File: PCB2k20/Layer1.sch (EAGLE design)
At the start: 279 parts, among them J1 XT30PB-F, J10 14AWG, J11 14AWG, J13 14AWG, J14 14AWG, J15 14AWG, J16 14AWG, J17 14AWG, J18 14AWG, J19 14AWG, J20 14AWG, J3 14AWG, J4 14AWG, J5 14AWG, J6 14AWG, J7 14AWG, J8 14AWG, J9 14AWG, Q1M1 AOD482, Q1M2 AOD482, Q1M3 AOD482, Q1M4 AOD482, U1M1 VNH5019, U1M2 VNH5019, U1M3 VNH5019, U1M4 VNH5019, X1 BM10B-SRSS-TB

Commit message: add gerbers, please everything turn out well!
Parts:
- added J21, U$29: 14AWG, JH:14AWG
- 2L1: value SWPA8040/10uH -> 10uH
- 3C4: value 1500uF -> 1000uF/63V
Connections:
- net GND: now also J21.1, U$29.1
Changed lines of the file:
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@@
 <part name="2C3" library="JH" library_urn="urn:adsk.eagle:library:6027132" deviceset="CAPACITOR" device="0603" package3d_urn="urn:adsk.eagle:package:15441226/3" value="10.0nF"/>
 <part name="2D1" library="SparkFun-DiscreteSemi" library_urn="urn:adsk.eagle:library:514" deviceset="DIODE-SCHOTTKY" device="-B340A" package3d_urn="urn:adsk.eagle:package:38443/1" value="3A/40V/500mV"/>
-<part name="2L1" library="JH" library_urn="urn:adsk.eagle:library:6027132" deviceset="INDUCTOR" device="SWPA8040" package3d_urn="urn:adsk.eagle:package:15402033/4" value="SWPA8040/10uH"/>
+<part name="2L1" library="JH" library_urn="urn:adsk.eagle:library:6027132" deviceset="INDUCTOR" device="SWPA8040" package3d_urn="urn:adsk.eagle:package:15402033/4" value="10uH"/>
 <part name="2R1" library="JH" library_urn="urn:adsk.eagle:library:6027132" deviceset="RESISTOR" device="0603" package3d_urn="urn:adsk.eagle:package:15441228/3" value="10k"/>
 <part name="2C4" library="rcl" library_urn="urn:adsk.eagle:library:334" deviceset="CPOL-US" device="D/7343-31R" package3d_urn="urn:adsk.eagle:package:23417/2" value="220uF"/>
@@
 <part name="SUPPLY25" library="SparkFun-PowerSymbols" library_urn="urn:adsk.eagle:library:530" deviceset="12V" device=""/>
 <part name="SUPPLY26" library="SparkFun-PowerSymbols" library_urn="urn:adsk.eagle:library:530" deviceset="3.3V" device=""/>
-<part name="CONN_M1" library="JH" library_urn="urn:adsk.eagle:library:6027132" deviceset="XT30" device="PB-F" package3d_urn="urn:adsk.eagle:package:15925142/4"/>
+<part name="CONN_M1" library="JH" library_urn="urn:adsk.eagle:library:6027132" deviceset="XT30" device="PB-F" package3d_urn="urn:adsk.eagle:package:15925142/7"/>
 <part name="U$4" library="JH" library_urn="urn:adsk.eagle:library:6027132" deviceset="74LVC2G" device="" package3d_urn="urn:adsk.eagle:package:16673544/1"/>
 <part name="U$5" library="JH" library_urn="urn:adsk.eagle:library:6027132" deviceset="74LVC2G" device="" package3d_urn="urn:adsk.eagle:package:16673544/1"/>
@@
 <part name="D2M2" library="SparkFun-LED" library_urn="urn:adsk.eagle:library:529" deviceset="LED-RED" device="0603" package3d_urn="urn:adsk.eagle:package:39354/1" value="RED"/>
 <part name="R12M2" library="JH" library_urn="urn:adsk.eagle:library:6027132" deviceset="RESISTOR" device="0603" package3d_urn="urn:adsk.eagle:package:15441228/3" value="4.7k"/>
-<part name="CONN_M2" library="JH" library_urn="urn:adsk.eagle:library:6027132" deviceset="XT30" device="PB-F" package3d_urn="urn:adsk.eagle:package:15925142/4"/>
+<part name="CONN_M2" library="JH" library_urn="urn:adsk.eagle:library:6027132" deviceset="XT30" device="PB-F" package3d_urn="urn:adsk.eagle:package:15925142/7"/>
 <part name="D1M3" library="SparkFun-LED" library_urn="urn:adsk.eagle:library:529" deviceset="LED-GREEN" device="0603" package3d_urn="urn:adsk.eagle:package:39354/1" value="GREEN"/>
 <part name="D2M3" library="SparkFun-LED" library_urn="urn:adsk.eagle:library:529" deviceset="LED-RED" device="0603" package3d_urn="urn:adsk.eagle:package:39354/1" value="RED"/>
 <part name="R12M3" library="JH" library_urn="urn:adsk.eagle:library:6027132" deviceset="RESISTOR" device="0603" package3d_urn="urn:adsk.eagle:package:15441228/3" value="4.7k"/>
-<part name="CONN_M3" library="JH" library_urn="urn:adsk.eagle:library:6027132" deviceset="XT30" device="PB-F" package3d_urn="urn:adsk.eagle:package:15925142/4"/>
+<part name="CONN_M3" library="JH" library_urn="urn:adsk.eagle:library:6027132" deviceset="XT30" device="PB-F" package3d_urn="urn:adsk.eagle:package:15925142/7"/>
 <part name="D1M4" library="SparkFun-LED" library_urn="urn:adsk.eagle:library:529" deviceset="LED-GREEN" device="0603" package3d_urn="urn:adsk.eagle:package:39354/1" value="GREEN"/>
 <part name="D2M4" library="SparkFun-LED" library_urn="urn:adsk.eagle:library:529" deviceset="LED-RED" device="0603" package3d_urn="urn:adsk.eagle:package:39354/1" value="RED"/>
 <part name="R12M4" library="JH" library_urn="urn:adsk.eagle:library:6027132" deviceset="RESISTOR" device="0603" package3d_urn="urn:adsk.eagle:package:15441228/3" value="4.7k"/>
-<part name="CONN_M4" library="JH" library_urn="urn:adsk.eagle:library:6027132" deviceset="XT30" device="PB-F" package3d_urn="urn:adsk.eagle:package:15925142/4"/>
+<part name="CONN_M4" library="JH" library_urn="urn:adsk.eagle:library:6027132" deviceset="XT30" device="PB-F" package3d_urn="urn:adsk.eagle:package:15925142/7"/>
 <part name="GND24" library="SparkFun-PowerSymbols" library_urn="urn:adsk.eagle:library:530" deviceset="GND" device=""/>
 <part name="SUPPLY29" library="SparkFun-PowerSymbols" library_urn="urn:adsk.eagle:library:530" deviceset="VCC_2" device=""/>
@@
 <part name="SUPPLY31" library="SparkFun-PowerSymbols" deviceset="3.3V" device=""/>
 <part name="GND26" library="SparkFun-PowerSymbols" library_urn="urn:adsk.eagle:library:530" deviceset="GND" device=""/>
-<part name="3C4" library="JH" library_urn="urn:adsk.eagle:library:6027132" deviceset="1000UF-CAP" device="" package3d_urn="urn:adsk.eagle:package:7103959/4" value="1500uF"/>
+<part name="3C4" library="JH" library_urn="urn:adsk.eagle:library:6027132" deviceset="1000UF-CAP" device="" package3d_urn="urn:adsk.eagle:package:7103959/4" value="1000uF/63V"/>
 <part name="1PT37" library="SparkFun-Sensors" deviceset="LIGHT_SENSOR" device="ALS"/>
 <part name="1PT38" library="SparkFun-Sensors" deviceset="LIGHT_SENSOR" device="ALS"/>
@@
 <part name="3C7" library="JH" library_urn="urn:adsk.eagle:library:6027132" deviceset="CAPACITOR" device="0603" package3d_urn="urn:adsk.eagle:package:15441226/3" value="1500pF"/>
 <part name="3R10" library="JH" library_urn="urn:adsk.eagle:library:6027132" deviceset="RESISTOR" device="0603" package3d_urn="urn:adsk.eagle:package:15441228/3" value="20"/>
-<part name="J1" library="JH" library_urn="urn:adsk.eagle:library:6027132" deviceset="XT30" device="PB-F" package3d_urn="urn:adsk.eagle:package:15925142/4"/>
+<part name="J1" library="JH" library_urn="urn:adsk.eagle:library:6027132" deviceset="XT30" device="PB-F" package3d_urn="urn:adsk.eagle:package:15925142/7"/>
 <part name="U$6" library="SparkFun-PowerSymbols" library_urn="urn:adsk.eagle:library:530" deviceset="VCCA" device=""/>
 <part name="U$7" library="SparkFun-PowerSymbols" library_urn="urn:adsk.eagle:library:530" deviceset="VCCA" device=""/>
@@
 <part name="U$27" library="JH" library_urn="urn:adsk.eagle:library:6027132" deviceset="18AWG" device="" package3d_urn="urn:adsk.eagle:package:16754415/1"/>
 <part name="U$28" library="JH" library_urn="urn:adsk.eagle:library:6027132" deviceset="18AWG" device="" package3d_urn="urn:adsk.eagle:package:16754415/1"/>
+<part name="U$29" library="JH" library_urn="urn:adsk.eagle:library:6027132" deviceset="14AWG" device="" package3d_urn="urn:adsk.eagle:package:16673531/1"/>
+<part name="J21" library="JH" library_urn="urn:adsk.eagle:library:6027132" deviceset="14AWG" device="" package3d_urn="urn:adsk.eagle:package:16673531/1"/>
 </parts>
 <sheets>
@@
 <attribute name="NAME" x="180.34" y="156.972" size="1.778" layer="95" font="vector" rot="R180"/>
 </instance>
+<instance part="U$29" gate="G$1" x="17.78" y="15.24" smashed="yes">
+<attribute name="VALUE" x="15.24" y="10.414" size="1.778" layer="96" font="vector"/>
+<attribute name="NAME" x="15.24" y="18.288" size="1.778" layer="95" font="vector"/>
+</instance>
 </instances>
 <busses>
@@
 <wire x1="111.76" y1="15.24" x2="104.14" y2="15.24" width="0.1524" layer="91"/>
 <junction x="104.14" y="15.24"/>
+<pinref part="U$29" gate="G$1" pin="1"/>
+<wire x1="25.4" y1="15.24" x2="27.94" y2="15.24" width="0.1524" layer="91"/>
+<junction x="27.94" y="15.24"/>
 </segment>
 <segment>
@@
 <attribute name="VALUE" x="160.02" y="86.106" size="1.778" layer="96" align="top-center"/>
 </instance>
+<instance part="J21" gate="G$1" x="124.46" y="139.7" smashed="yes">
+<attribute name="VALUE" x="121.92" y="134.874" size="1.778" layer="96" font="vector"/>
+<attribute name="NAME" x="121.92" y="142.748" size="1.778" layer="95" font="vector"/>
+</instance>
 </instances>
 <busses>
@@
 <wire x1="134.62" y1="66.04" x2="134.62" y2="78.74" width="0.1524" layer="91"/>
 <wire x1="104.14" y1="142.24" x2="134.62" y2="142.24" width="0.1524" layer="91"/>
-<wire x1="134.62" y1="142.24" x2="134.62" y2="129.54" width="0.1524" layer="91"/>
+<wire x1="134.62" y1="142.24" x2="134.62" y2="139.7" width="0.1524" layer="91"/>
 <pinref part="J6" gate="G$1" pin="1"/>
+<wire x1="134.62" y1="139.7" x2="134.62" y2="129.54" width="0.1524" layer="91"/>
 <wire x1="134.62" y1="129.54" x2="134.62" y2="116.84" width="0.1524" layer="91"/>
 <wire x1="132.08" y1="129.54" x2="134.62" y2="129.54" width="0.1524" layer="91"/>
@@
 <wire x1="132.08" y1="66.04" x2="134.62" y2="66.04" width="0.1524" layer="91"/>
 <junction x="134.62" y="66.04"/>
+<pinref part="J21" gate="G$1" pin="1"/>
+<wire x1="132.08" y1="139.7" x2="134.62" y2="139.7" width="0.1524" layer="91"/>
+<junction x="134.62" y="139.7"/>
 </segment>
 <segment>

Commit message: update values
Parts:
- 1C1, 1C3, 1C5: value (none) -> 0.1uF
- 1C13, 1C14, 1C15, 1C16, 1C17, 1C2, 1C4, 1C6: value (none) -> 1uF
- 1R1: value 15 -> 0.39
- 1R12, 1R13, 1R14, 1R15, 1R16, 1R3, 1R5, 1R7: value (none) -> 3k
- 1R2, 1R4, 1R6: value (none) -> 10k
- 2C4: value 220uF -> 330uF
- 2D1: value 3A/40V/500mV -> SS54
- C3M1, C3M2, C3M3, C3M4: value 1.0uF -> 1uF
- R1: value 300k -> 30k
- R11M1, R11M2, R11M3, R11M4, R2: value 100k -> 10k
- R3, R4: value (none) -> 4.7k
- R5, R6, R7, R8: value (none) -> 3.9k

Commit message: Change pullup resistor to value we alr have
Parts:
- R1M1, R1M2, R1M3, R1M4, R2M1, R2M2, R2M3, R2M4: value 3.3k -> 3.24k
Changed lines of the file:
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@@
 <drawing>
 <settings>
-<setting alwaysvectorfont="no"/>
+<setting alwaysvectorfont="yes"/>
 <setting verticaltext="up"/>
 </settings>
@@
 <part name="R6M1" library="JH" library_urn="urn:adsk.eagle:library:6027132" deviceset="RESISTOR" device="0603" package3d_urn="urn:adsk.eagle:package:15441228/3" value="1k"/>
 <part name="SUPPLY8" library="SparkFun-PowerSymbols" library_urn="urn:adsk.eagle:library:530" deviceset="3.3V" device=""/>
-<part name="R1M1" library="JH" library_urn="urn:adsk.eagle:library:6027132" deviceset="RESISTOR" device="0603" package3d_urn="urn:adsk.eagle:package:15441228/3" value="3.3k"/>
-<part name="R2M1" library="JH" library_urn="urn:adsk.eagle:library:6027132" deviceset="RESISTOR" device="0603" package3d_urn="urn:adsk.eagle:package:15441228/3" value="3.3k"/>
+<part name="R1M1" library="JH" library_urn="urn:adsk.eagle:library:6027132" deviceset="RESISTOR" device="0603" package3d_urn="urn:adsk.eagle:package:15441228/3" value="3.24k"/>
+<part name="R2M1" library="JH" library_urn="urn:adsk.eagle:library:6027132" deviceset="RESISTOR" device="0603" package3d_urn="urn:adsk.eagle:package:15441228/3" value="3.24k"/>
 <part name="R7M1" library="JH" library_urn="urn:adsk.eagle:library:6027132" deviceset="RESISTOR" device="0603" package3d_urn="urn:adsk.eagle:package:15441228/3" value="1k"/>
 <part name="R8M1" library="JH" library_urn="urn:adsk.eagle:library:6027132" deviceset="RESISTOR" device="0603" package3d_urn="urn:adsk.eagle:package:15441228/3" value="10k"/>
@@
 <part name="R6M2" library="JH" library_urn="urn:adsk.eagle:library:6027132" deviceset="RESISTOR" device="0603" package3d_urn="urn:adsk.eagle:package:15441228/3" value="1k"/>
 <part name="SUPPLY9" library="SparkFun-PowerSymbols" library_urn="urn:adsk.eagle:library:530" deviceset="3.3V" device=""/>
-<part name="R1M2" library="JH" library_urn="urn:adsk.eagle:library:6027132" deviceset="RESISTOR" device="0603" package3d_urn="urn:adsk.eagle:package:15441228/3" value="3.3k"/>
-<part name="R2M2" library="JH" library_urn="urn:adsk.eagle:library:6027132" deviceset="RESISTOR" device="0603" package3d_urn="urn:adsk.eagle:package:15441228/3" value="3.3k"/>
+<part name="R1M2" library="JH" library_urn="urn:adsk.eagle:library:6027132" deviceset="RESISTOR" device="0603" package3d_urn="urn:adsk.eagle:package:15441228/3" value="3.24k"/>
+<part name="R2M2" library="JH" library_urn="urn:adsk.eagle:library:6027132" deviceset="RESISTOR" device="0603" package3d_urn="urn:adsk.eagle:package:15441228/3" value="3.24k"/>
 <part name="R7M2" library="JH" library_urn="urn:adsk.eagle:library:6027132" deviceset="RESISTOR" device="0603" package3d_urn="urn:adsk.eagle:package:15441228/3" value="1k"/>
 <part name="R8M2" library="JH" library_urn="urn:adsk.eagle:library:6027132" deviceset="RESISTOR" device="0603" package3d_urn="urn:adsk.eagle:package:15441228/3" value="10k"/>
@@
 <part name="R6M3" library="JH" library_urn="urn:adsk.eagle:library:6027132" deviceset="RESISTOR" device="0603" package3d_urn="urn:adsk.eagle:package:15441228/3" value="1k"/>
 <part name="SUPPLY10" library="SparkFun-PowerSymbols" library_urn="urn:adsk.eagle:library:530" deviceset="3.3V" device=""/>
-<part name="R1M3" library="JH" library_urn="urn:adsk.eagle:library:6027132" deviceset="RESISTOR" device="0603" package3d_urn="urn:adsk.eagle:package:15441228/3" value="3.3k"/>
-<part name="R2M3" library="JH" library_urn="urn:adsk.eagle:library:6027132" deviceset="RESISTOR" device="0603" package3d_urn="urn:adsk.eagle:package:15441228/3" value="3.3k"/>
+<part name="R1M3" library="JH" library_urn="urn:adsk.eagle:library:6027132" deviceset="RESISTOR" device="0603" package3d_urn="urn:adsk.eagle:package:15441228/3" value="3.24k"/>
+<part name="R2M3" library="JH" library_urn="urn:adsk.eagle:library:6027132" deviceset="RESISTOR" device="0603" package3d_urn="urn:adsk.eagle:package:15441228/3" value="3.24k"/>
 <part name="R7M3" library="JH" library_urn="urn:adsk.eagle:library:6027132" deviceset="RESISTOR" device="0603" package3d_urn="urn:adsk.eagle:package:15441228/3" value="1k"/>
 <part name="R8M3" library="JH" library_urn="urn:adsk.eagle:library:6027132" deviceset="RESISTOR" device="0603" package3d_urn="urn:adsk.eagle:package:15441228/3" value="10k"/>
@@
 <part name="R6M4" library="JH" library_urn="urn:adsk.eagle:library:6027132" deviceset="RESISTOR" device="0603" package3d_urn="urn:adsk.eagle:package:15441228/3" value="1k"/>
 <part name="SUPPLY11" library="SparkFun-PowerSymbols" library_urn="urn:adsk.eagle:library:530" deviceset="3.3V" device=""/>
-<part name="R1M4" library="JH" library_urn="urn:adsk.eagle:library:6027132" deviceset="RESISTOR" device="0603" package3d_urn="urn:adsk.eagle:package:15441228/3" value="3.3k"/>
-<part name="R2M4" library="JH" library_urn="urn:adsk.eagle:library:6027132" deviceset="RESISTOR" device="0603" package3d_urn="urn:adsk.eagle:package:15441228/3" value="3.3k"/>
+<part name="R1M4" library="JH" library_urn="urn:adsk.eagle:library:6027132" deviceset="RESISTOR" device="0603" package3d_urn="urn:adsk.eagle:package:15441228/3" value="3.24k"/>
+<part name="R2M4" library="JH" library_urn="urn:adsk.eagle:library:6027132" deviceset="RESISTOR" device="0603" package3d_urn="urn:adsk.eagle:package:15441228/3" value="3.24k"/>
 <part name="R7M4" library="JH" library_urn="urn:adsk.eagle:library:6027132" deviceset="RESISTOR" device="0603" package3d_urn="urn:adsk.eagle:package:15441228/3" value="1k"/>
 <part name="R8M4" library="JH" library_urn="urn:adsk.eagle:library:6027132" deviceset="RESISTOR" device="0603" package3d_urn="urn:adsk.eagle:package:15441228/3" value="10k"/>

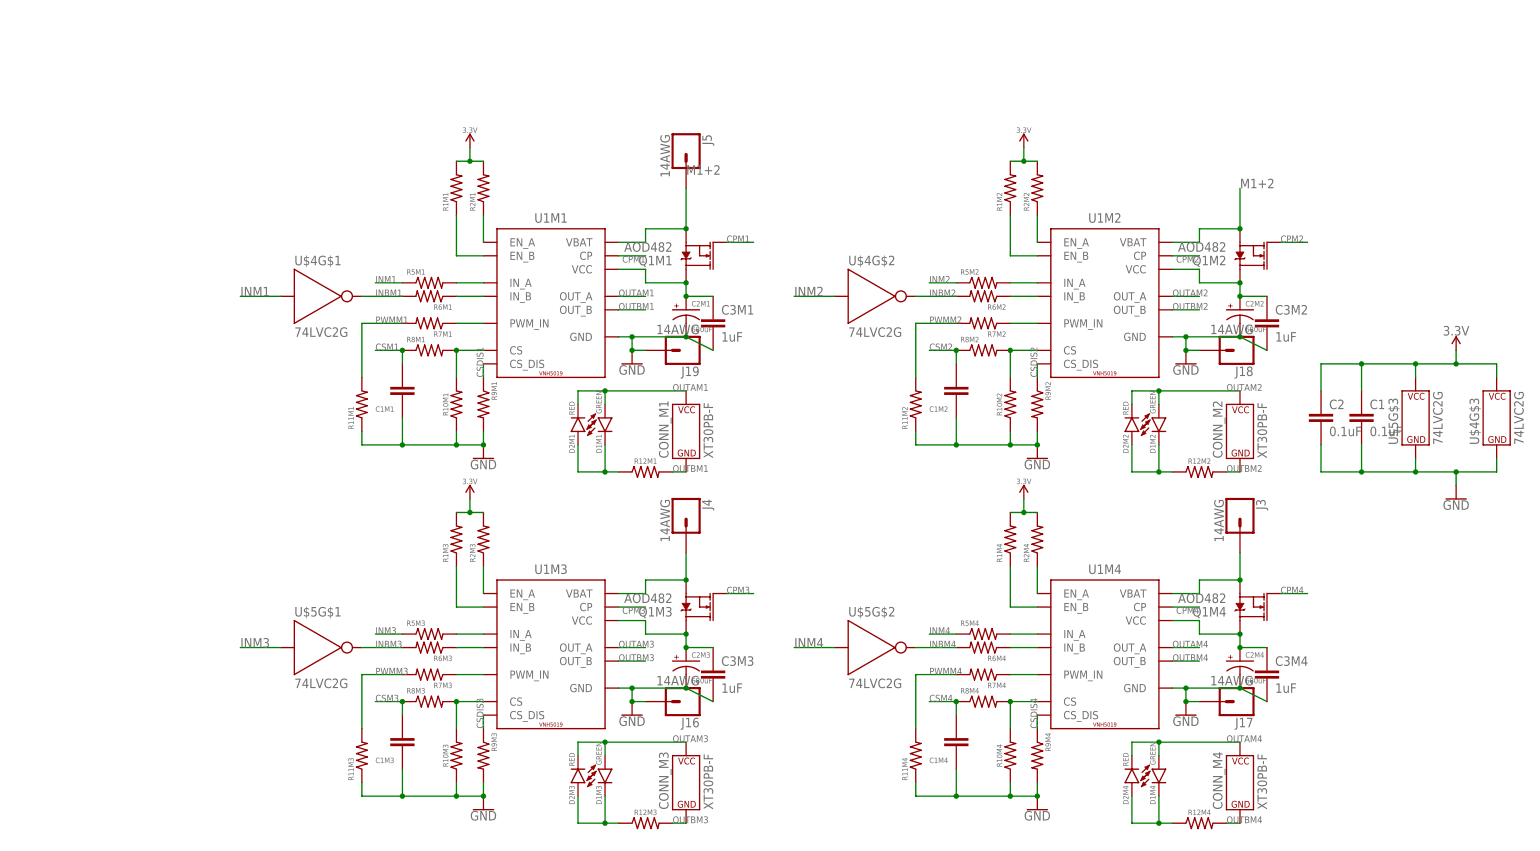
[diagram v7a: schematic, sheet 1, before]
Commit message: BROKEN VERSION for 3d models
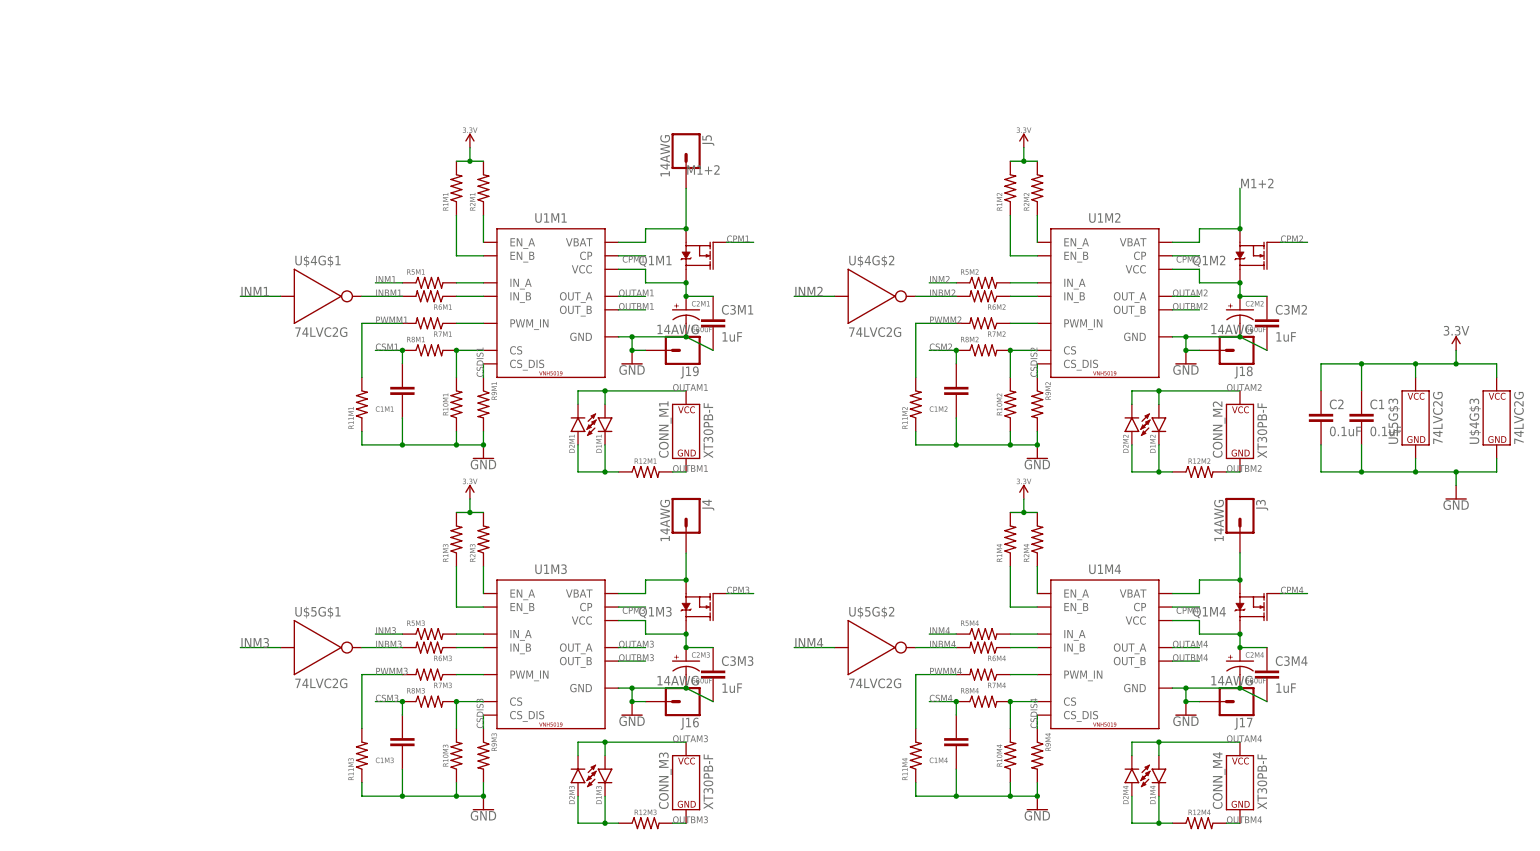
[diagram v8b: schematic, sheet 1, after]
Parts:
- removed LIGHT, S1: (no value), SparkFun-Switches:SWITCH-SPDT-PTH-11.6X4.0MM-LOCK
- added U$30, U$31: SWITCH_SPDT_TH, JH:SWITCH_SPDT_TH
- 1D0: device SparkFun-LED:LED-BLUE0603 -> JH:LED0603
- 1OSC: device SparkFun-Clocks:CRYSTALSMD-5X3.2-2PAD -> JH:CRYSTAL_5032
- 1PT1, 1PT10, 1PT11, 1PT12, 1PT13, 1PT14, 1PT15, 1PT16, 1PT17, 1PT18, 1PT19, 1PT2, 1PT20, 1PT21, 1PT22, 1PT23, 1PT24, 1PT25, 1PT26, 1PT27, 1PT28, 1PT29, 1PT3, 1PT30, 1PT31, 1PT32, 1PT33, 1PT34, 1PT35, 1PT36, 1PT37, 1PT38, 1PT4, 1PT5, 1PT6, 1PT7, 1PT8, 1PT9: value LIGHT_SENSORALS -> LIGHT_SENSOR_ALS; device SparkFun-Sensors:LIGHT_SENSORALS -> JH:LIGHT_SENSOR_ALS
- 2D1: device SparkFun-DiscreteSemi:DIODE-SCHOTTKY-B340A -> JH:DIODE-SCHOTTKY
- 3C3: value 100uF -> CAPACITOR_POL_10X10.5MM; device SparkFun-Capacitors:100UF-POLAR-10X10.5-63V-20% -> JH:CAPACITOR_POL_10X10.5MM
- 3D4: value 1N4728 -> DIODE-ZENER; device diode:1N4728 -> JH:DIODE-ZENER
- 3Q3: device SparkFun-DiscreteSemi:MOSFET-NCH-FQP30N06L -> JH:MOSFET-NCH-TO220V
- 3Q4: device SparkFun-DiscreteSemi:MOSFET-NCH-AO3404A -> JH:MOSFET-NCH-SOT23-3
- D1M1, D1M2, D1M3, D1M4: device SparkFun-LED:LED-GREEN0603 -> JH:LED0603
- D2M1, D2M2, D2M3, D2M4: device SparkFun-LED:LED-RED0603 -> JH:LED0603
- FB1, FB2: value 30Ω/1.8A -> FERRITE_BEAD; device SparkFun-Coils:FERRITE_BEAD-0603 -> JH:FERRITE_BEAD
- J2: device SparkFun-Connectors:CONN_04 -> Connectors:CONN_04LOCK
- MOUSE: device SparkFun-Connectors:CONN_08LOCK -> Connectors:CONN_08LOCK
- Q1M1, Q1M2, Q1M3, Q1M4: device SparkFun-DiscreteSemi:MOSFET-NCH-FDD8780 -> JH:MOSFET-NCH-DPAK
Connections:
- net 3.3V: now also U$31.O; no longer S1.O
- net 3.3V_MCU: now also U$31.P; no longer S1.P
- net 3.3V_PROG: now also U$31.S; no longer S1.S
- net N$3: now also U$30.S; no longer LIGHT.S
- net N$36: now also U$30.P; no longer LIGHT.P
